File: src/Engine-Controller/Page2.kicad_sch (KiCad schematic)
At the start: 29 parts, among them P2 Solid Prop Cont, P4 Micro_SD_Card, P5 USB, P6 140-504-415-000, P9 5015680807, Q1 QS5U17TR, U11 TS391IYLT, U4 SST25VF040B-50-4I-S2AE-T, U5 CP2102-GMR(QFN28)

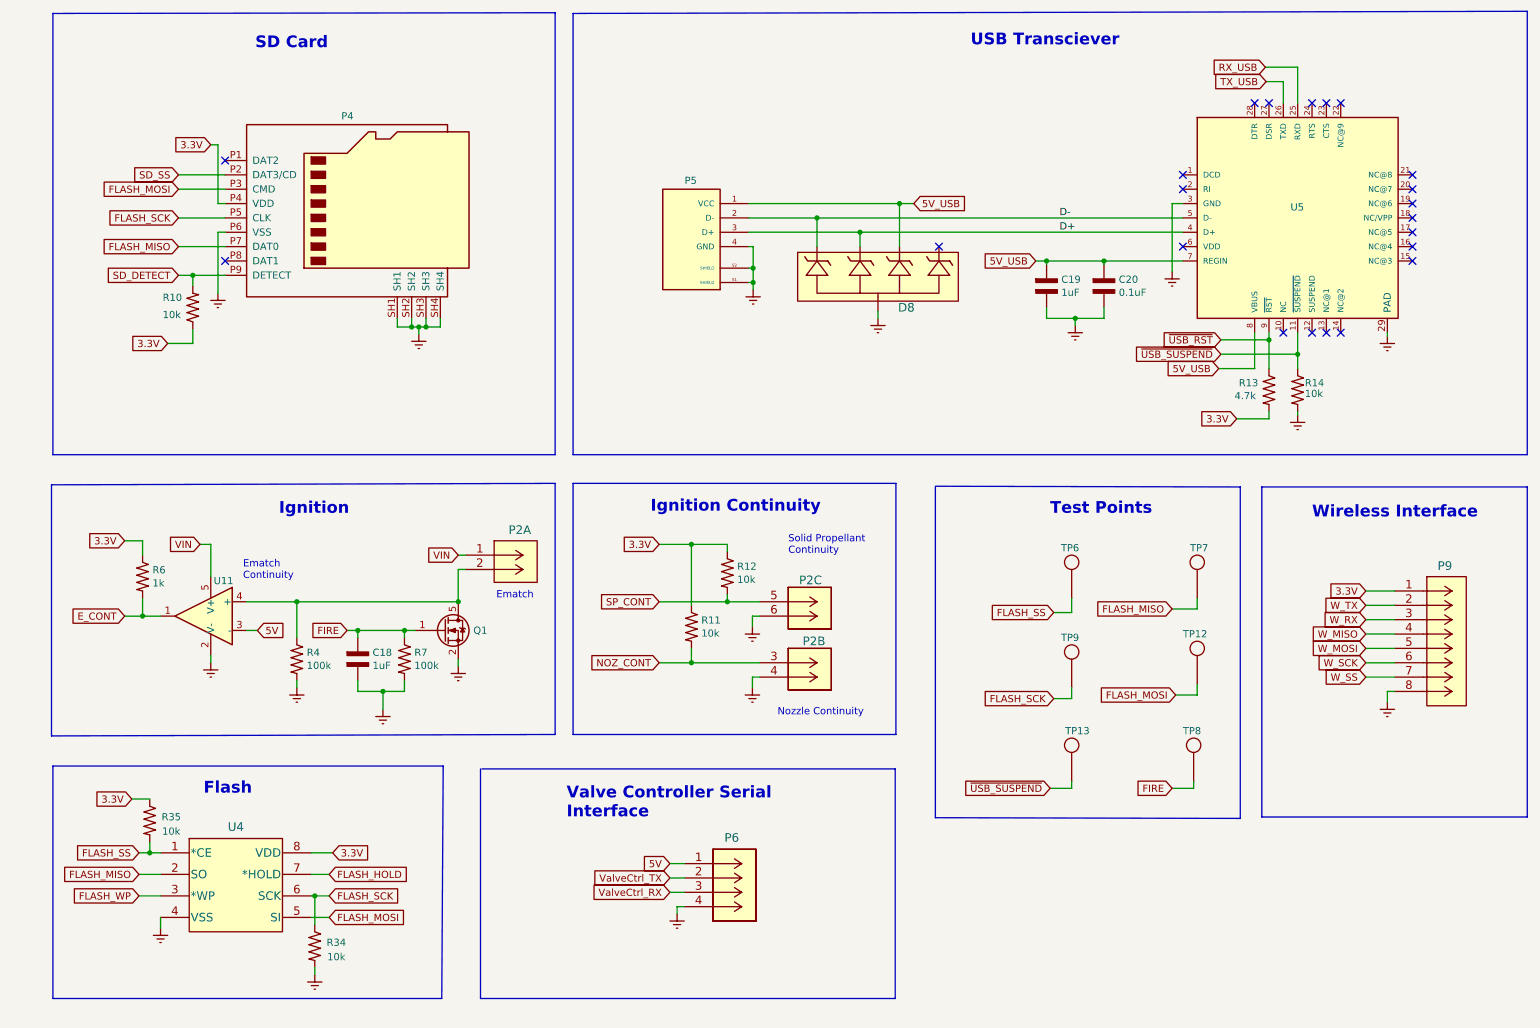
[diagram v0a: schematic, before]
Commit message: resolved all ERC schematic issues
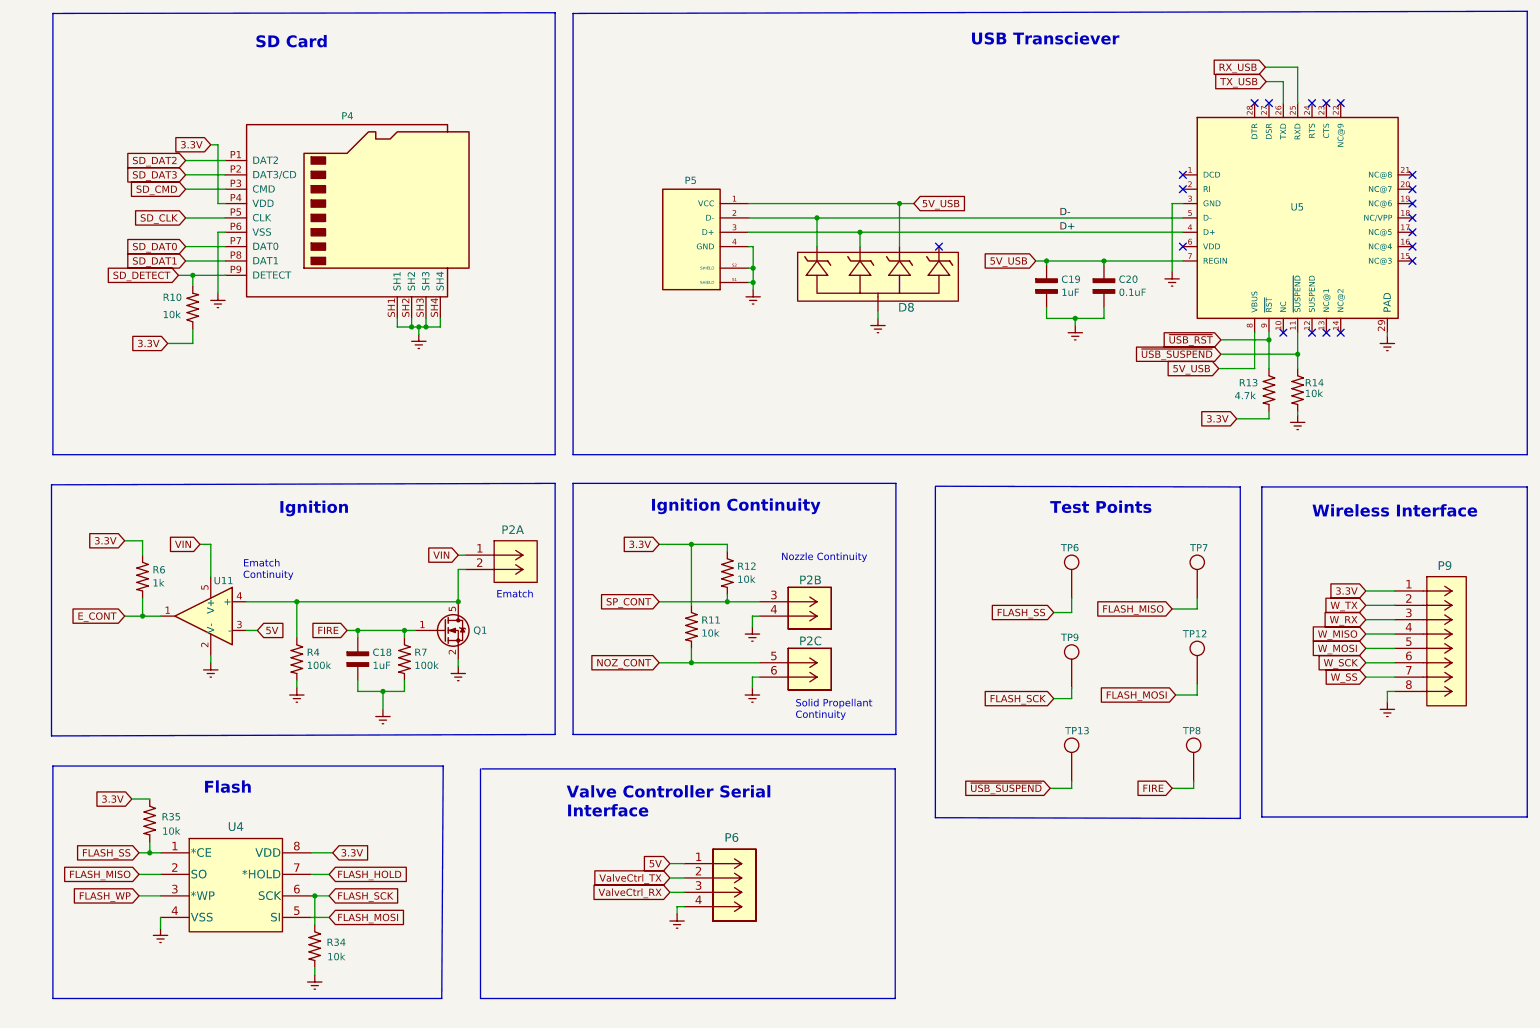
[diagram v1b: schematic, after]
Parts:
- removed P2: Solid Prop Cont, Engine-Controller:TE_282837-6, symbol Engine-Controller:IgnitionScrewTerminal
- added P2: 282837-6, Engine-Controller:282837-6, symbol Engine-Controller:282837-6
- D8: footprint SOD-123FL_MCC -> Engine-Controller:SP0504BAHTG
- P4: footprint Engine-Controller:GCT_MEM2075-00-140-01-A -> Engine-Controller:MEM2075-00-140-01-A
- P5: footprint BEL_SS-52300-001 -> Engine-Controller:USB-TypeB
- P6: footprint CONN_4840.2201_SCH -> Engine-Controller:140-504-415-000
- P9: footprint 66953-005LF_AMP -> Engine-Controller:5015680807
- Q1: footprint Package_TO_SOT_THT:TO-92_Inline -> Engine-Controller:QS5U17TR
- U11: footprint (none) -> Engine-Controller:TS391IYLT
- U4: footprint SOIC8_S2A_SST_MCH -> Engine-Controller:SST25VF040B-50-4I-S2AE-T
- U5: footprint QFN28G_0.5-5X5MM -> Engine-Controller:CP2012-GMR
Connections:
- net Earth: now also P2.4 (6), P2.6
- net FLASH_MISO: no longer P4.P7 (DAT0)
- net FLASH_MOSI: no longer P4.P3 (CMD)
- net FLASH_SCK: no longer P4.P5 (CLK)
- net NOZ_CONT: now also P2.5
- net SP_CONT: now also P2.3 (5)
- net VIN: now also P2.1 (5)
- net at Q1.5 (D), R4.1, U11.4 (+): now also P2.2 (6)
- net SD_DAT2: now reaches P4.P1 (DAT2)
- net SD_DAT1: now reaches P4.P8 (DAT1)
- net SD_SS renamed SD_DAT3
- new net SD_CLK: P4.P5 (CLK)
- new net SD_CMD: P4.P3 (CMD)
- new net SD_DAT0: P4.P7 (DAT0)
- no-connect marks 22 -> 20

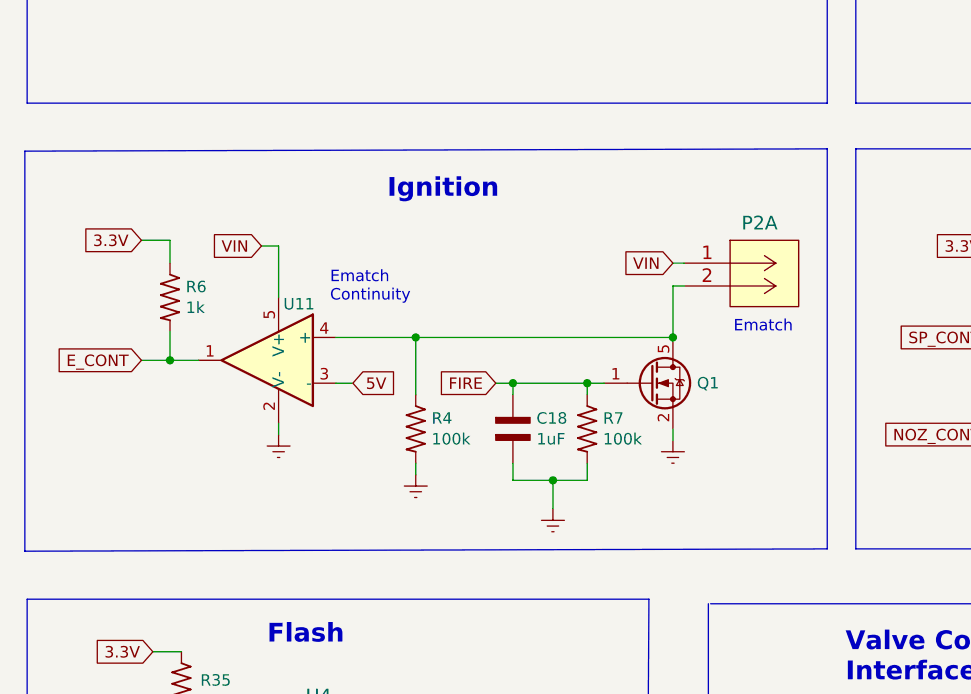
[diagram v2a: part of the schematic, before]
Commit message: added safety switch to schematic
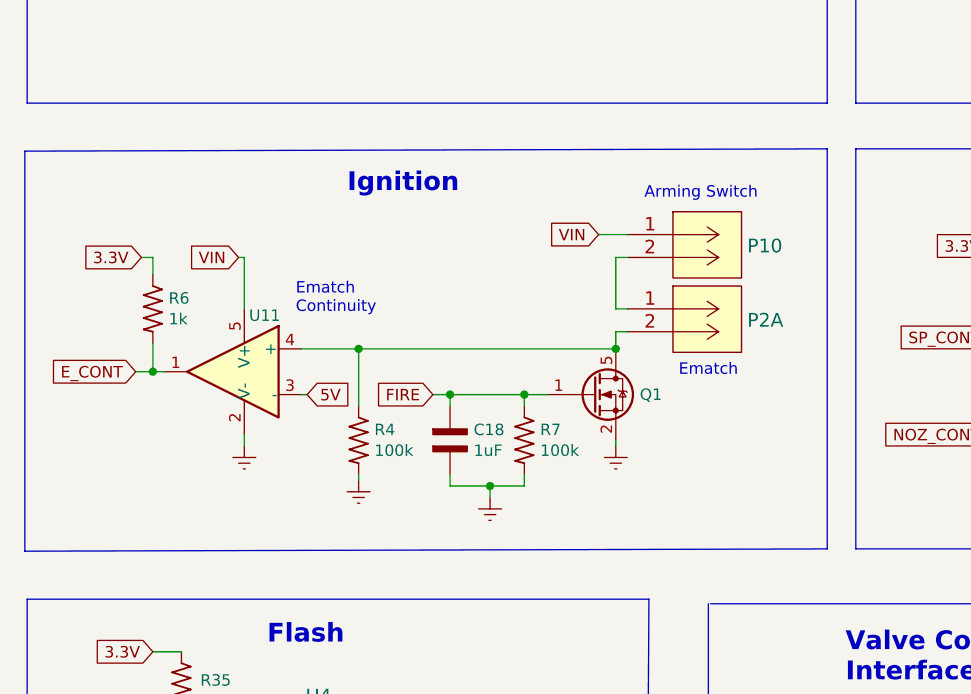
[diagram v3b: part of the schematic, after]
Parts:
- added P10: 282837-2, Engine-Controller:282837-2, symbol Engine-Controller:282837-2
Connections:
- net VIN: now also P10.1 (5); no longer P2.1 (5)
- new net: P10.2 (6), P2.1 (5)
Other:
- note added: "Arming Switch"
- moved on the sheet: C18, P2A, Q1, R4, R6, R7, U11

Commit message: routed rev4
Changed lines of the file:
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@@
     (effects (font (size 2.08 2.08) (thickness 0.416) bold) (justify left bottom))
   )
-  (text "Nozzle Continuity\n" (at 149.225 115.57 0)
+  (text "Nozzle Continuity\n" (at 150.495 141.605 0)
     (effects (font (size 1.27 1.27)) (justify left bottom))
   )
-  (text "Solid Propellant\nContinuity\n" (at 151.765 143.51 0)
+  (text "Solid Propellant\nContinuity\n" (at 149.86 115.57 0)
     (effects (font (size 1.27 1.27)) (justify left bottom))
   )

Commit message: minor lib file changes
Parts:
- R6: value 1k -> 10k
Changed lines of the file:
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@@
     (effects (font (size 1.27 1.27)) (justify left bottom))
   )
-  (text "Ignition" (at 55.88 106.68 0)
+  (text "Ignition" (at 59.055 106.68 0)
     (effects (font (size 2.08 2.08) (thickness 0.416) bold) (justify left bottom))
   )
@@
       (effects (font (size 1.27 1.27)) (justify left))
     )
-    (property "Value" "1k" (id 1) (at 36.0426 120.523 90)
+    (property "Value" "10k" (id 1) (at 36.0426 120.523 90)
       (effects (font (size 1.27 1.27)) (justify left))
     )

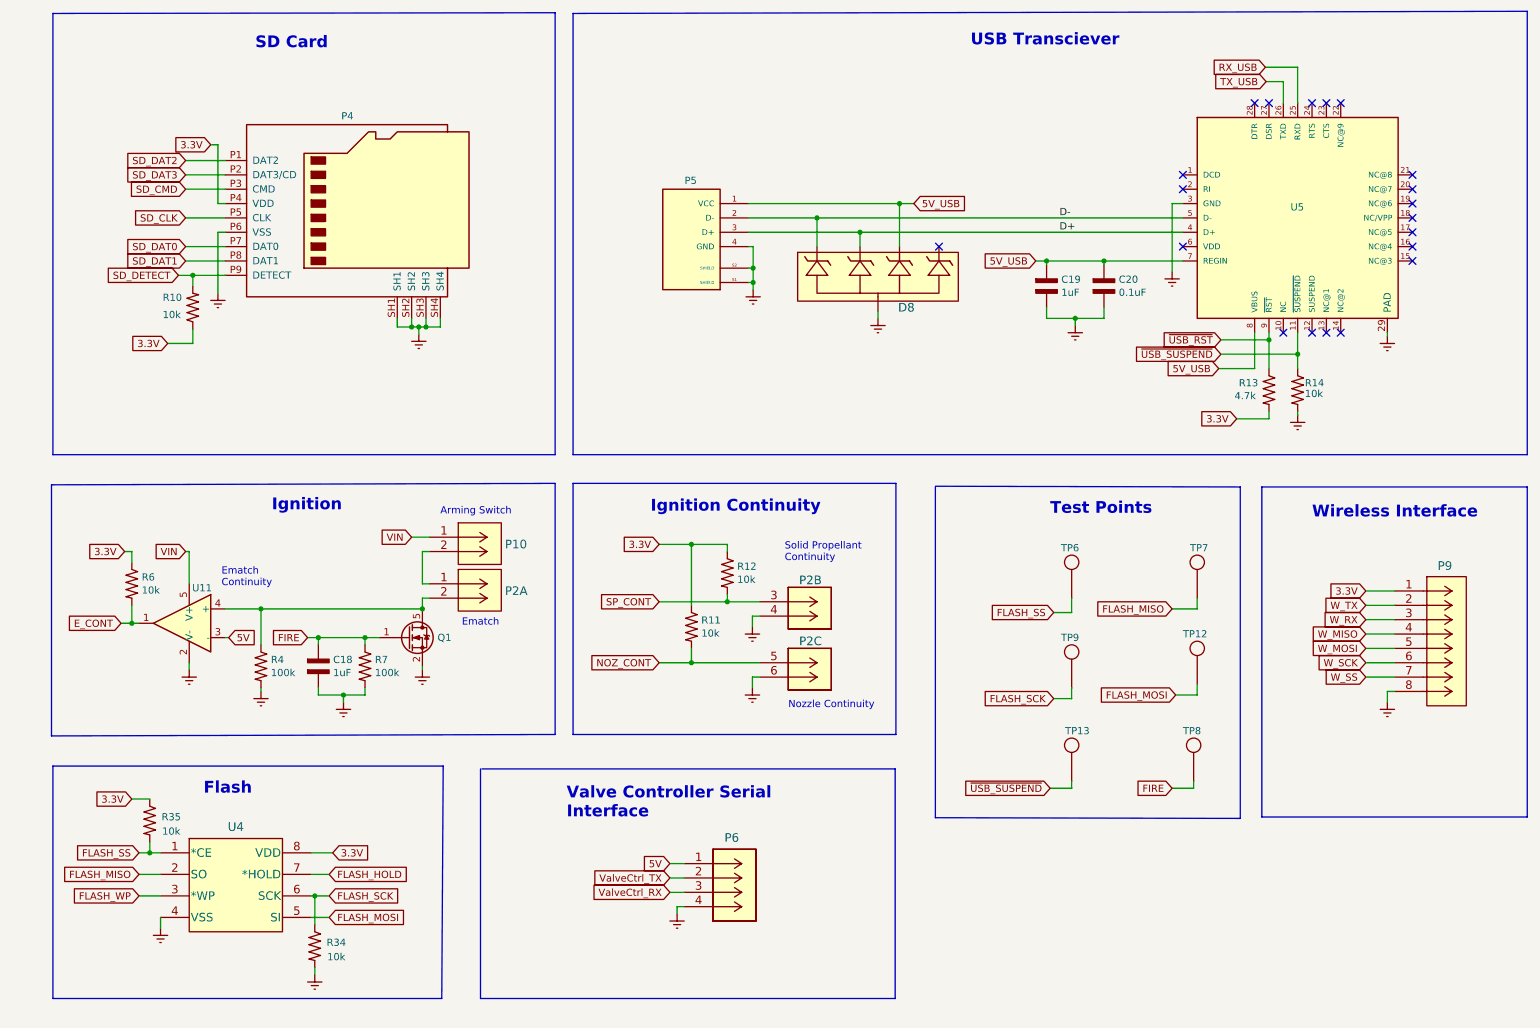
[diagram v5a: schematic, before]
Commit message: copied over 5.0/5.1 updates from Gain-Calc branch
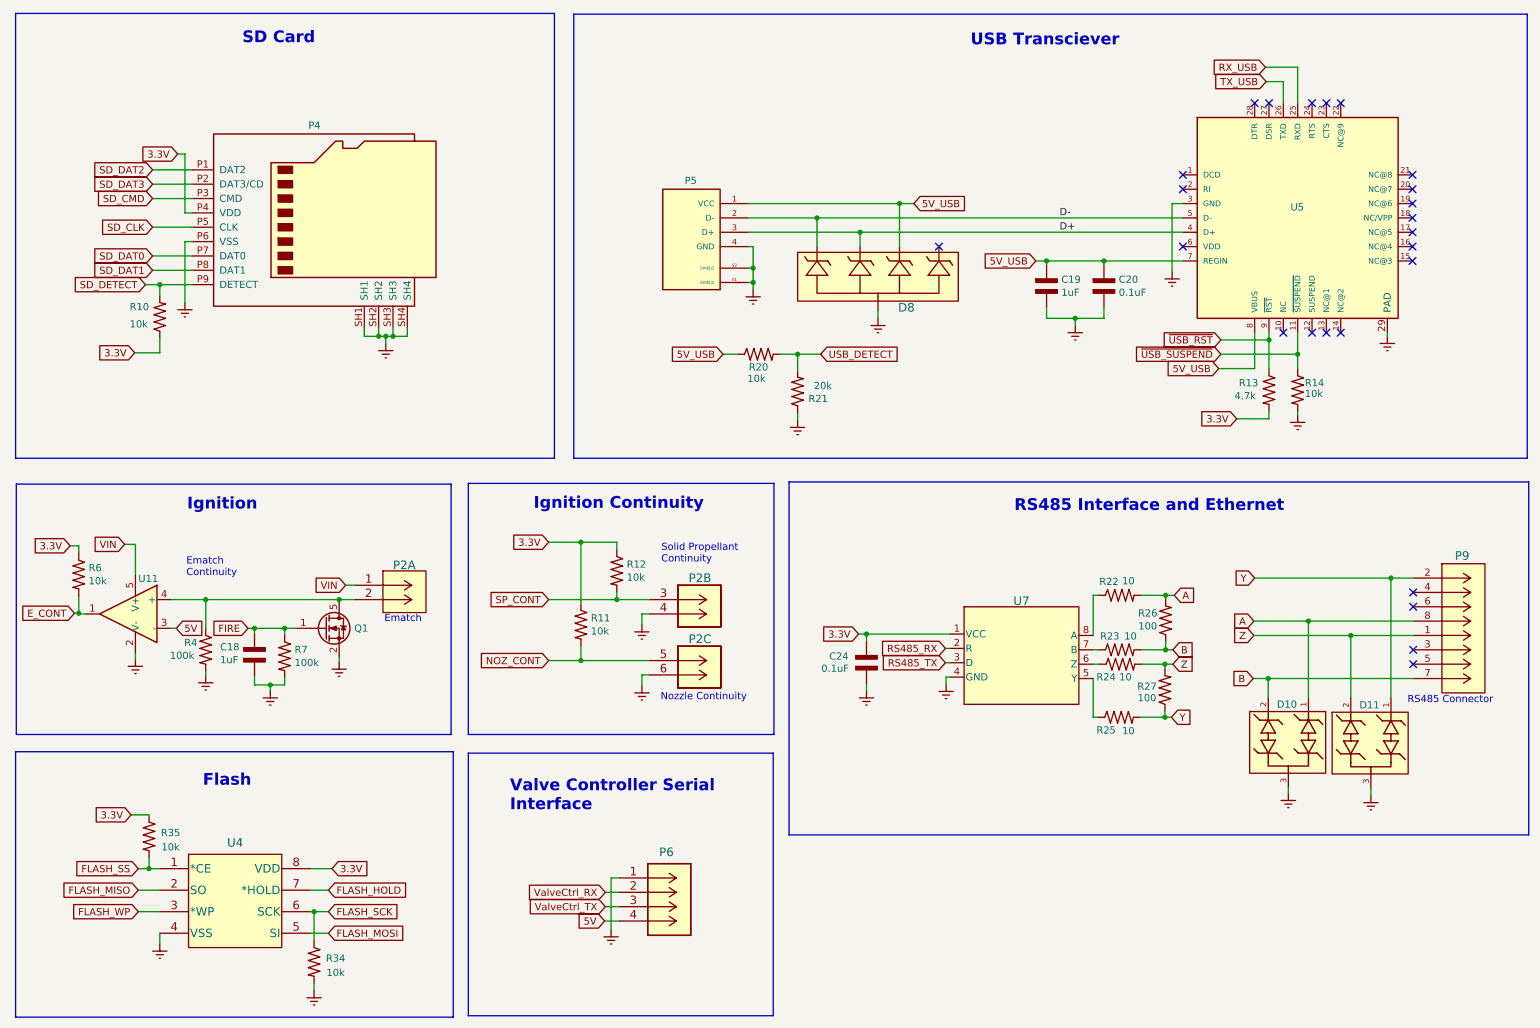
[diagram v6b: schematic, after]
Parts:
- removed P10: 282837-2, Engine-Controller:282837-2, symbol Engine-Controller:282837-2
- removed P9: 5015680807, Engine-Controller:5015680807, symbol Engine-Controller:5015680807
- removed TP12, TP13, TP6, TP7, TP8, TP9: TP, Engine-Controller:TP, symbol Engine-Controller:TP
- added C24: 0.1uF, Engine-Controller:CAP_0603, symbol Engine-Controller:CAP_0603
- added D10, D11: SMBJ36CA-13-F, Engine-Controller:CDSOT23-SM712, symbol Engine-Controller:CDSOT23-SM712
- added P9: 54602-908LF, Engine-Controller:54602-908LF, symbol Engine-Controller:54602-908LF
- added R20: 10k, Engine-Controller:RES_0603, symbol Engine-Controller:RES_0603
- added R21: 20k, Engine-Controller:RES_0603, symbol Engine-Controller:RES_0603
- added R22, R23, R24, R25: 10, Engine-Controller:RES_0603, symbol Engine-Controller:RES_0603
- added R26, R27: 100, Engine-Controller:RES_0603, symbol Engine-Controller:RES_0603
- added U7: SN65HVD71DR, Engine-Controller:SN65HVD71DR, symbol Engine-Controller:SN65HVD71DR
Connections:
- net 3.3V: now also C24.2, U7.1 (VCC)
- net 5V: now also P6.4; no longer P6.1 (+12V)
- net 5V_USB: now also R20.1
- net Earth: now also P6.1 (+12V), C24.1, D10.3, D11.3, R21.1, U7.4 (GND); no longer P6.4
- net VIN: now also P2.1 (5)
- net ValveCtrl_RX: now also P6.2 (GND); no longer P6.3
- net ValveCtrl_TX: now also P6.3; no longer P6.2 (GND)
- new net: R25.1, U7.5 (Y)
- new net: R24.1, U7.6 (Z)
- new net: R23.1, U7.7 (B)
- new net: R22.1, U7.8 (A)
- new net A: D10.1, P9.8, R22.2, R26.2
- new net B: D10.2, P9.7, R23.2, R26.1
- new net RS485_RX: U7.2 (R)
- new net RS485_TX: U7.3 (D)
- new net USB_DETECT: R20.2, R21.2
- new net Y: D11.1, P9.2, R25.2, R27.1
- new net Z: D11.2, P9.1, R24.2, R27.2
- no-connect marks 20 -> 24
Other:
- note added: "RS485 Connector"
- note added: "RS485 Interface and Ethernet"
- note removed: "Arming Switch"
- note removed: "Test Points"
- note removed: "Wireless Interface"
- moved on the sheet: C18, P2A, P2B, P2C, P4, P6, Q1, R10, R11, R12, R34, R35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
